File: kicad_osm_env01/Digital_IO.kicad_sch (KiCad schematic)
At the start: 22 parts, among them U18 MIC94073YC6, U20 MIC94073YC6

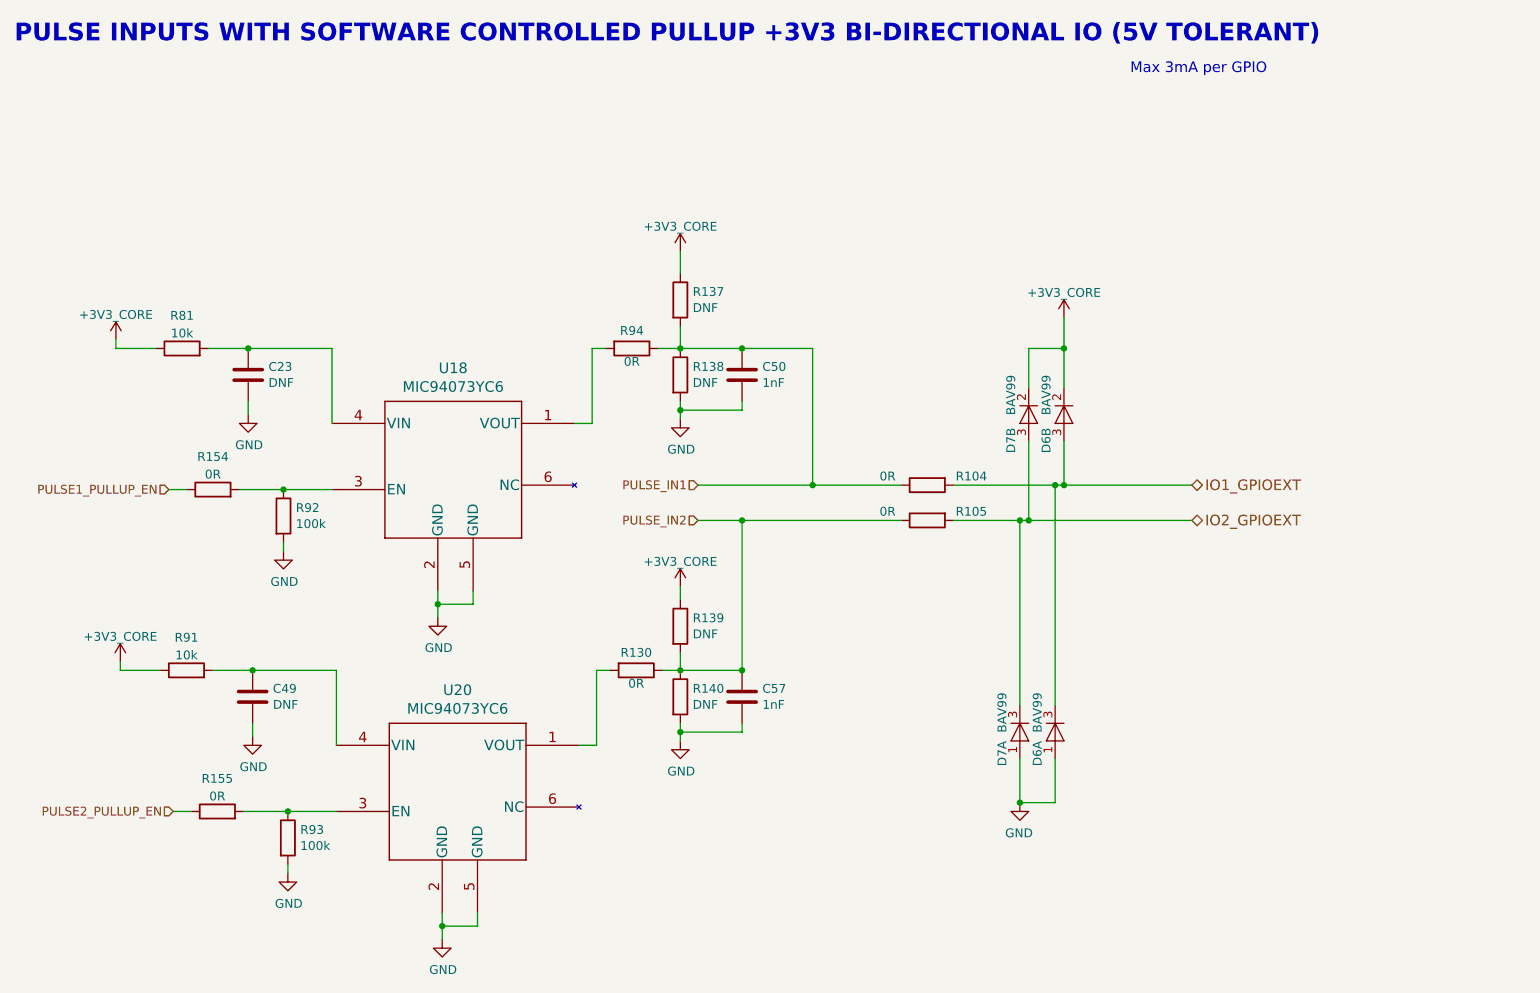
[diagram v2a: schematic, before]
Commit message: removed io module and 5V regulator
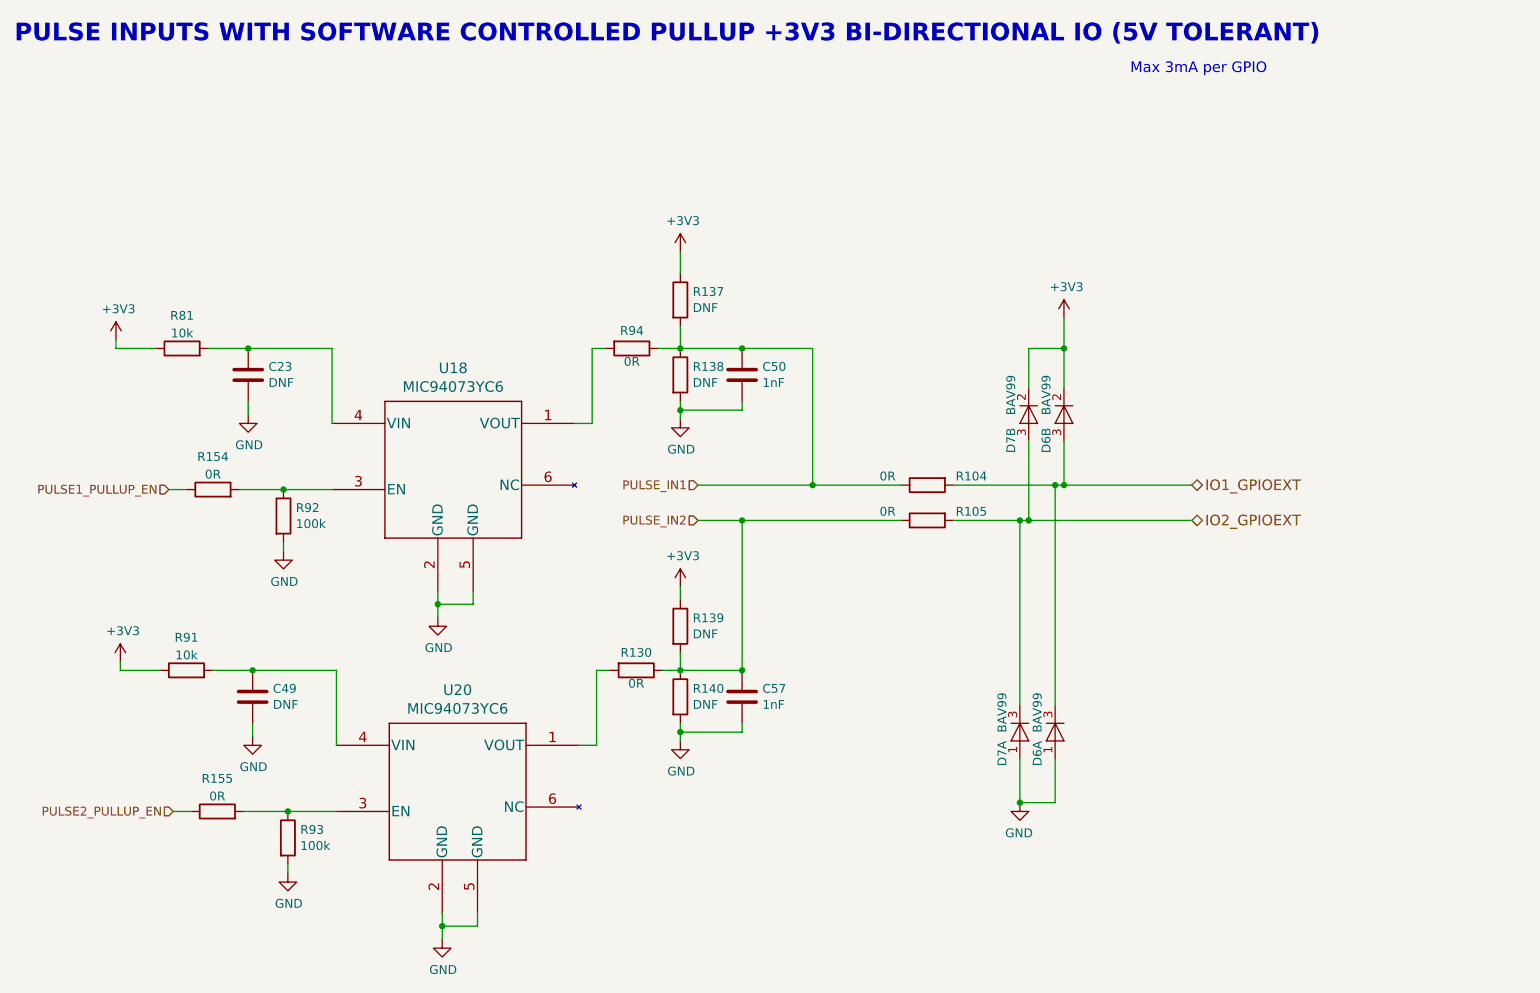
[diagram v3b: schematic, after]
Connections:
- net +3V3_CORE renamed +3V3
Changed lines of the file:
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@@
+    )
+  )
+  (symbol (lib_id "power:+3V3") (at 210.185 60.96 0) (unit 1)
+    (in_bom yes) (on_board yes) (dnp no)
+    (property "Reference" "#PWR0142" (at 210.185 64.77 0)
+      (effects (font (size 1.27 1.27)) hide)
+    )
+    (property "Value" "+3V3" (at 210.566 56.5658 0)
+      (effects (font (size 1.27 1.27)))
+    )
+    (property "Footprint" "" (at 210.185 60.96 0)
+      (effects (font (size 1.27 1.27)) hide)
+    )
+    (property "Datasheet" "" (at 210.185 60.96 0)
+      (effects (font (size 1.27 1.27)) hide)
+    )
+    (pin "1")
+    (instances
+      (project "OSM_env01"
+        (path "/ab8b0540-9c9f-4195-88f5-7bed0b0a8ed6"
+          (reference "#PWR0142") (unit 1)
+        )
+        (path "/ab8b0540-9c9f-4195-88f5-7bed0b0a8ed6/00000000-0000-0000-0000-0000608f4675/00000000-0000-0000-0000-000060920857"
+          (reference "#PWR052") (unit 1)
+        )
+      )
     )
   )
@@
         (path "/ab8b0540-9c9f-4195-88f5-7bed0b0a8ed6/00000000-0000-0000-0000-0000608f4675/00000000-0000-0000-0000-000060920857"
           (reference "R154") (unit 1)
+        )
+      )
+    )
+  )
+  (symbol (lib_id "power:+3V3") (at 74.295 110.49 0) (unit 1)
+    (in_bom yes) (on_board yes) (dnp no)
+    (property "Reference" "#PWR0142" (at 74.295 114.3 0)
+      (effects (font (size 1.27 1.27)) hide)
+    )
+    (property "Value" "+3V3" (at 74.676 106.0958 0)
+      (effects (font (size 1.27 1.27)))
+    )
+    (property "Footprint" "" (at 74.295 110.49 0)
+      (effects (font (size 1.27 1.27)) hide)
+    )
+    (property "Datasheet" "" (at 74.295 110.49 0)
+      (effects (font (size 1.27 1.27)) hide)
+    )
+    (pin "1")
+    (instances
+      (project "OSM_env01"
+        (path "/ab8b0540-9c9f-4195-88f5-7bed0b0a8ed6"
+          (reference "#PWR0142") (unit 1)
+        )
+        (path "/ab8b0540-9c9f-4195-88f5-7bed0b0a8ed6/00000000-0000-0000-0000-0000608f4675/00000000-0000-0000-0000-000060920857"
+          (reference "#PWR08") (unit 1)
         )
       )
@@
     )
   )
-  (symbol (lib_id "Devtank:+3V3_CORE") (at 154.94 99.695 0) (unit 1)
-    (in_bom yes) (on_board yes) (dnp no) (fields_autoplaced)
-    (property "Reference" "#PWR045" (at 154.94 103.505 0)
-      (effects (font (size 1.27 1.27)) hide)
-    )
-    (property "Value" "+3V3_CORE" (at 154.94 96.1192 0)
-      (effects (font (size 1.27 1.27)))
-    )
-    (property "Footprint" "" (at 154.94 99.695 0)
-      (effects (font (size 1.27 1.27)))
-    )
-    (property "Datasheet" "" (at 154.94 99.695 0)
-      (effects (font (size 1.27 1.27)))
-    )
-    (pin "1")
-    (instances
-      (project "OSM_env01"
-        (path "/ab8b0540-9c9f-4195-88f5-7bed0b0a8ed6/00000000-0000-0000-0000-0000608f4675/00000000-0000-0000-0000-000060920857"
-          (reference "#PWR045") (unit 1)
+  (symbol (lib_id "power:+3V3") (at 73.66 64.135 0) (unit 1)
+    (in_bom yes) (on_board yes) (dnp no)
+    (property "Reference" "#PWR0142" (at 73.66 67.945 0)
+      (effects (font (size 1.27 1.27)) hide)
+    )
+    (property "Value" "+3V3" (at 74.041 59.7408 0)
+      (effects (font (size 1.27 1.27)))
+    )
+    (property "Footprint" "" (at 73.66 64.135 0)
+      (effects (font (size 1.27 1.27)) hide)
+    )
+    (property "Datasheet" "" (at 73.66 64.135 0)
+      (effects (font (size 1.27 1.27)) hide)
+    )
+    (pin "1")
+    (instances
+      (project "OSM_env01"
+        (path "/ab8b0540-9c9f-4195-88f5-7bed0b0a8ed6"
+          (reference "#PWR0142") (unit 1)
+        )
+        (path "/ab8b0540-9c9f-4195-88f5-7bed0b0a8ed6/00000000-0000-0000-0000-0000608f4675/00000000-0000-0000-0000-000060920857"
+          (reference "#PWR06") (unit 1)
         )
       )
@@
         (path "/ab8b0540-9c9f-4195-88f5-7bed0b0a8ed6/00000000-0000-0000-0000-0000608f4675/00000000-0000-0000-0000-000060920857"
           (reference "R137") (unit 1)
+        )
+      )
+    )
+  )
+  (symbol (lib_id "power:+3V3") (at 154.94 51.435 0) (unit 1)
+    (in_bom yes) (on_board yes) (dnp no)
+    (property "Reference" "#PWR0142" (at 154.94 55.245 0)
+      (effects (font (size 1.27 1.27)) hide)
+    )
+    (property "Value" "+3V3" (at 155.321 47.0408 0)
+      (effects (font (size 1.27 1.27)))
+    )
+    (property "Footprint" "" (at 154.94 51.435 0)
+      (effects (font (size 1.27 1.27)) hide)
+    )
+    (property "Datasheet" "" (at 154.94 51.435 0)
+      (effects (font (size 1.27 1.27)) hide)
+    )
+    (pin "1")
+    (instances
+      (project "OSM_env01"
+        (path "/ab8b0540-9c9f-4195-88f5-7bed0b0a8ed6"
+          (reference "#PWR0142") (unit 1)
+        )
+        (path "/ab8b0540-9c9f-4195-88f5-7bed0b0a8ed6/00000000-0000-0000-0000-0000608f4675/00000000-0000-0000-0000-000060920857"
+          (reference "#PWR09") (unit 1)
         )
       )
@@
     )
   )
+  (symbol (lib_id "power:+3V3") (at 154.94 99.695 0) (unit 1)
+    (in_bom yes) (on_board yes) (dnp no)
+    (property "Reference" "#PWR0142" (at 154.94 103.505 0)
+      (effects (font (size 1.27 1.27)) hide)
+    )
+    (property "Value" "+3V3" (at 155.321 95.3008 0)
+      (effects (font (size 1.27 1.27)))
+    )
+    (property "Footprint" "" (at 154.94 99.695 0)
+      (effects (font (size 1.27 1.27)) hide)
+    )
+    (property "Datasheet" "" (at 154.94 99.695 0)
+      (effects (font (size 1.27 1.27)) hide)
+    )
+    (pin "1")
+    (instances
+      (project "OSM_env01"
+        (path "/ab8b0540-9c9f-4195-88f5-7bed0b0a8ed6"
+          (reference "#PWR0142") (unit 1)
+        )
+        (path "/ab8b0540-9c9f-4195-88f5-7bed0b0a8ed6/00000000-0000-0000-0000-0000608f4675/00000000-0000-0000-0000-000060920857"
+          (reference "#PWR045") (unit 1)
+        )
+      )
+    )
+  )
   (symbol (lib_id "power:GND") (at 97.79 94.615 0) (unit 1)
     (in_bom yes) (on_board yes) (dnp no)
@@
         (path "/ab8b0540-9c9f-4195-88f5-7bed0b0a8ed6/00000000-0000-0000-0000-0000608f4675/00000000-0000-0000-0000-000060920857"
           (reference "R94") (unit 1)
-        )
-      )
-    )
-  )
-  (symbol (lib_id "Devtank:+3V3_CORE") (at 154.94 51.435 0) (unit 1)
-    (in_bom yes) (on_board yes) (dnp no) (fields_autoplaced)
-    (property "Reference" "#PWR09" (at 154.94 55.245 0)
-      (effects (font (size 1.27 1.27)) hide)
-    )
-    (property "Value" "+3V3_CORE" (at 154.94 47.8592 0)
-      (effects (font (size 1.27 1.27)))
-    )
-    (property "Footprint" "" (at 154.94 51.435 0)
-      (effects (font (size 1.27 1.27)))
-    )
-    (property "Datasheet" "" (at 154.94 51.435 0)
-      (effects (font (size 1.27 1.27)))
-    )
-    (pin "1")
-    (instances
-      (project "OSM_env01"
-        (path "/ab8b0540-9c9f-4195-88f5-7bed0b0a8ed6/00000000-0000-0000-0000-0000608f4675/00000000-0000-0000-0000-000060920857"
-          (reference "#PWR09") (unit 1)
         )
       )
@@
         )
       )
-    )
-  )
-  (symbol (lib_id "Devtank:+3V3_CORE") (at 73.66 64.135 0) (unit 1)
-    (in_bom yes) (on_board yes) (dnp no) (fields_autoplaced)
-    (property "Reference" "#PWR06" (at 73.66 67.945 0)
-      (effects (font (size 1.27 1.27)) hide)
-    )
-    (property "Value" "+3V3_CORE" (at 73.66 60.5592 0)
-      (effects (font (size 1.27 1.27)))
-    )
-    (property "Footprint" "" (at 73.66 64.135 0)
-      (effects (font (size 1.27 1.27)))
-    )
-    (property "Datasheet" "" (at 73.66 64.135 0)
-      (effects (font (size 1.27 1.27)))
-    )
-    (pin "1")
-    (instances
-      (project "OSM_env01"
-        (path "/ab8b0540-9c9f-4195-88f5-7bed0b0a8ed6/00000000-0000-0000-0000-0000608f4675/00000000-0000-0000-0000-000060920857"
-          (reference "#PWR06") (unit 1)
-        )
-      )
-    )
-  )
-  (symbol (lib_id "Devtank:+3V3_CORE") (at 210.185 60.96 0) (unit 1)
-    (in_bom yes) (on_board yes) (dnp no) (fields_autoplaced)
-    (property "Reference" "#PWR055" (at 210.185 64.77 0)
-      (effects (font (size 1.27 1.27)) hide)
-    )
-    (property "Value" "+3V3_CORE" (at 210.185 57.3842 0)
-      (effects (font (size 1.27 1.27)))
-    )
-    (property "Footprint" "" (at 210.185 60.96 0)
-      (effects (font (size 1.27 1.27)))
-    )
-    (property "Datasheet" "" (at 210.185 60.96 0)
-      (effects (font (size 1.27 1.27)))
-    )
-    (pin "1")
-    (instances
-      (project "OSM_env01"
-        (path "/ab8b0540-9c9f-4195-88f5-7bed0b0a8ed6/00000000-0000-0000-0000-0000608f4675/00000000-0000-0000-0000-000060920857"
-          (reference "#PWR055") (unit 1)
-        )
-      )
-    )
-  )
-  (symbol (lib_id "Devtank:+3V3_CORE") (at 74.295 110.49 0) (unit 1)
-    (in_bom yes) (on_board yes) (dnp no) (fields_autoplaced)
-    (property "Reference" "#PWR08" (at 74.295 114.3 0)
-      (effects (font (size 1.27 1.27)) hide)
-    )
-    (property "Value" "+3V3_CORE" (at 74.295 106.9142 0)
-      (effects (font (size 1.27 1.27)))
-    )
-    (property "Footprint" "" (at 74.295 110.49 0)
-      (effects (font (size 1.27 1.27)))
-    )
-    (property "Datasheet" "" (at 74.295 110.49 0)
-      (effects (font (size 1.27 1.27)))
-    )
-    (pin "1")
-    (instances
-      (project "OSM_env01"
-        (path "/ab8b0540-9c9f-4195-88f5-7bed0b0a8ed6/00000000-0000-0000-0000-0000608f4675/00000000-0000-0000-0000-000060920857"
-          (reference "#PWR08") (unit 1)
-        )
-      )
